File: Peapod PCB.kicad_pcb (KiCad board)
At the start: 2 copper layers, 16 parts, among them J1 CONN_01X01, J2 CONN_01X02, J3 CONN_01X06, J5 CONN_01X01, J6 CONN_01X01, J7 CONN_01X02, U1 ESP8266

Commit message: Changed main file for layout
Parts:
- moved BT1 38.2 mm to (193.0, 39.4)
- moved J1 35.6 mm to (179.1, 30.5)
- moved BTN1 22.2 mm to (182.9, 48.3), turned to 180 degrees
- moved BTN3 21.6 mm to (190.5, 48.3), turned to 180 degrees
- moved R3 21.0 mm to (205.7, 43.2), turned to 180 degrees
- moved R5 18.9 mm to (205.7, 38.1)
- moved J7 17.7 mm to (200.7, 48.9)
- moved R4 13.1 mm to (205.7, 40.6)
- moved R2 11.7 mm to (179.1, 39.4)
- moved J6 11.0 mm to (210.2, 48.9)
- moved J3 9.09 mm to (218.4, 31.1), turned to 270 degrees
- moved J5 8.47 mm to (216.5, 48.9)
- moved R1 7.41 mm to (179.1, 35.6)
- moved BTN2 3.81 mm to (175.3, 48.3), turned to 180 degrees
- moved J2 2.84 mm to (168.9, 30.5)
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
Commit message: changed things
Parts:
- moved BTN2 6.35 mm to (168.9, 48.3)
- moved BTN1 3.81 mm to (179.1, 48.3)
- moved BTN3 1.27 mm to (189.2, 48.3)
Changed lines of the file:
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@@
   )
   (module mod:Pushbutton (layer F.Cu)
-    (at 182.88 48.26 180)
+    (at 179.07 48.26 180)
     (fp_text reference BTN1 (at 0 0.5 180) (layer F.SilkS)
       (effects (font (size 1 1) (thickness 0.15)))
@@
   )
   (module mod:Pushbutton (layer F.Cu)
-    (at 175.26 48.26 180)
+    (at 168.91 48.26 180)
     (fp_text reference BTN2 (at 0 0.5 180) (layer F.SilkS)
       (effects (font (size 1 1) (thickness 0.15)))
@@
   )
   (module mod:Pushbutton (layer F.Cu)
-    (at 190.5 48.26 180)
+    (at 189.23 48.26 180)
     (fp_text reference BTN3 (at 0 0.5 180) (layer F.SilkS)
       (effects (font (size 1 1) (thickness 0.15)))

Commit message: made vias and tracks
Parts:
- moved J7 11.4 mm to (189.2, 49.5)
- moved J6 10.8 mm to (199.4, 49.5)
- moved BTN3 10.2 mm to (179.1, 47.0)
- moved J5 9.55 mm to (207.0, 49.5)
- moved BTN2 8.98 mm to (170.2, 39.4)
- moved BTN1 8.98 mm to (170.2, 47.0)
- moved R5 5.08 mm to (205.7, 43.2)
- moved BT1 5.08 mm to (188.0, 39.4)
- moved R3 2.54 mm to (205.7, 40.6)
- moved R4 2.54 mm to (205.7, 38.1)
- moved J3 2.29 mm to (217.2, 33.0)
- moved J2 1.27 mm to (170.2, 30.5)
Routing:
- net +3V3: track 0.00 -> 94.8 mm
- net Net-(J5-Pad1): track 0.00 -> 72.5 mm, vias 0 -> 2
- net Net-(BTN1-Pad2): track 0.00 -> 21.5 mm, vias 0 -> 2
- net Net-(J6-Pad1): track 0.00 -> 20.8 mm, vias 0 -> 2
- net Net-(J7-Pad1): track 0.00 -> 19.5 mm
- net Net-(BTN2-Pad2): track 0.00 -> 17.6 mm
- net Net-(R1-Pad1): track 0.00 -> 15.4 mm, vias 0 -> 2
- net Net-(J3-Pad4): track 0.00 -> 13.0 mm, vias 0 -> 2
- net Net-(J3-Pad5): track 0.00 -> 11.4 mm
- net Net-(BTN3-Pad2): track 0.00 -> 11.1 mm, vias 0 -> 2
- net Net-(J1-Pad1): track 0.00 -> 5.64 mm, vias 0 -> 1

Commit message: made fill zones
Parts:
- turned R1 to 180 degrees
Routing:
- net (no net): track 0.00 -> 31.4 mm
- net Net-(J5-Pad1): track 72.5 -> 58.9 mm
- net Net-(R1-Pad1): track 15.4 -> 1.81 mm, vias 2 -> 0
- net Net-(R5-Pad1): track 0.00 -> 5.83 mm
- net Net-(R3-Pad2): track 0.00 -> 5.56 mm
- net Net-(J7-Pad1): track 19.5 -> 24.8 mm
- net Net-(J2-Pad1): track 0.00 -> 1.27 mm
- net Net-(J1-Pad1): vias 1 -> 0
- added copper zone on F.Cu, net GND

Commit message: fixed stuff
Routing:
- net Net-(R1-Pad1): track 1.81 -> 13.8 mm, vias 0 -> 1
- net (no net): track 31.4 -> 21.2 mm
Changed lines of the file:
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@@
   (general
     (links 40)
-    (no_connects 18)
+    (no_connects 17)
     (area 154.9176 20.282599 222.719902 54.8674)
     (thickness 1.6002)
     (drawings 0)
-    (tracks 88)
+    (tracks 92)
     (zones 0)
     (modules 16)
@@
     )
   )
-  (segment (start 177.8 39.37) (end 177.8 38.1) (width 0.635) (layer B.Cu) (net 0))
-  (segment (start 177.8 38.1) (end 184.15 31.75) (width 0.635) (layer B.Cu) (net 0))
   (segment (start 185.42 29.21) (end 185.42 35.56) (width 0.635) (layer B.Cu) (net 0))
   (segment (start 180.34 30.48) (end 185.42 35.56) (width 0.635) (layer B.Cu) (net 0))
@@
   (segment (start 192.31 37.21) (end 199.42 37.21) (width 0.635) (layer F.Cu) (net 14))
   (segment (start 192.23 37.29) (end 192.31 37.21) (width 0.635) (layer F.Cu) (net 14))
-  (segment (start 183.61 31.21) (end 185.42 31.21) (width 0.635) (layer F.Cu) (net 15))
+  (segment (start 185.42 31.21) (end 182.975 31.21) (width 0.635) (layer F.Cu) (net 15) (status 400000))
+  (segment (start 182.245 35.56) (end 180.42 35.56) (width 0.635) (layer F.Cu) (net 15) (status 800000))
+  (segment (start 182.245 31.94) (end 182.245 35.56) (width 0.635) (layer F.Cu) (net 15))
+  (segment (start 182.975 31.21) (end 182.245 31.94) (width 0.635) (layer F.Cu) (net 15))
+  (via (at 180.42 35.56) (size 0.6858) (drill 0.3302) (layers F.Cu B.Cu) (net 15) (status C00000))
+  (segment (start 180.42 35.56) (end 177.8 38.18) (width 0.635) (layer B.Cu) (net 15) (status 400000))
+  (segment (start 177.8 38.18) (end 177.8 39.37) (width 0.635) (layer B.Cu) (net 15))
   (segment (start 204.39 40.64) (end 203.2 40.64) (width 0.635) (layer F.Cu) (net 16))
   (segment (start 201.77 39.21) (end 199.42 39.21) (width 0.635) (layer F.Cu) (net 16))

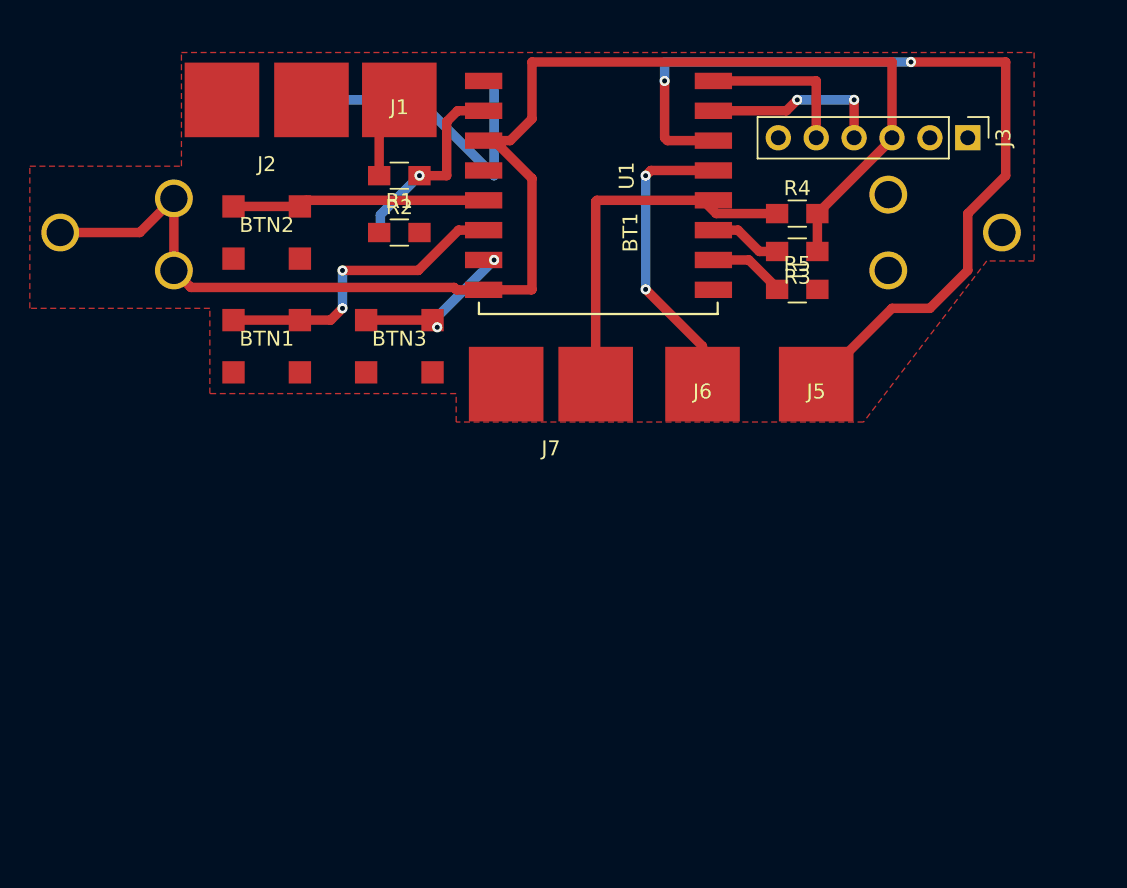
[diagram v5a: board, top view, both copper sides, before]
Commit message: Moved routing on the lines
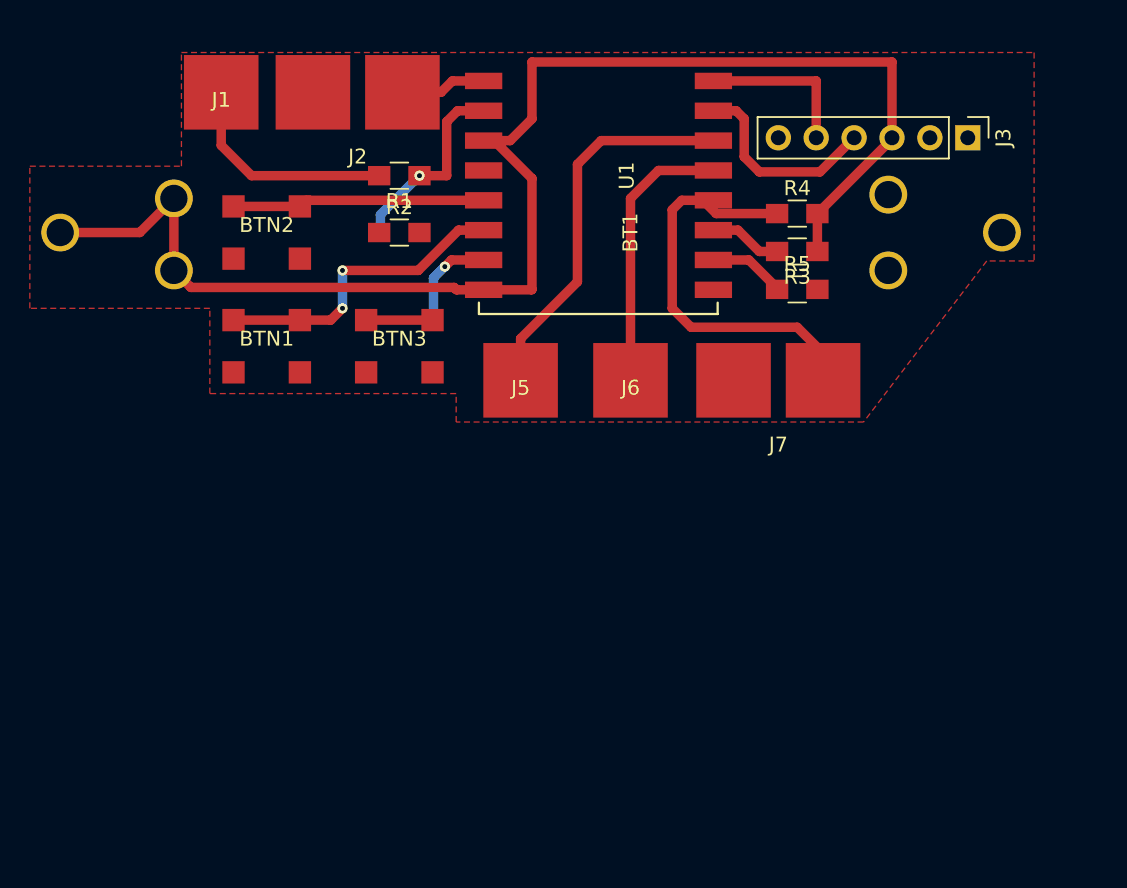
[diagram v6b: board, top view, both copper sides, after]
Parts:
- moved J5 19.8 mm to (187.2, 49.3)
- moved J7 15.2 mm to (204.5, 49.3)
- moved J1 11.9 mm to (167.1, 30.0)
- moved J2 6.12 mm to (176.3, 30.0)
- moved J6 4.83 mm to (194.6, 49.3)
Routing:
- net Net-(J5-Pad1): track 58.9 -> 25.1 mm, vias 2 -> 0
- net (no net): track 21.2 -> 0.00 mm
- net Net-(J1-Pad1): track 5.64 -> 16.9 mm
- net Net-(J2-Pad1): track 1.27 -> 7.73 mm
- net Net-(J7-Pad1): track 24.8 -> 27.4 mm
- net Net-(J6-Pad1): track 20.8 -> 19.1 mm, vias 2 -> 0
- net Net-(J3-Pad4): track 13.0 -> 14.3 mm, vias 2 -> 0
- net Net-(BTN3-Pad2): track 11.1 -> 11.6 mm, vias 2 -> 1

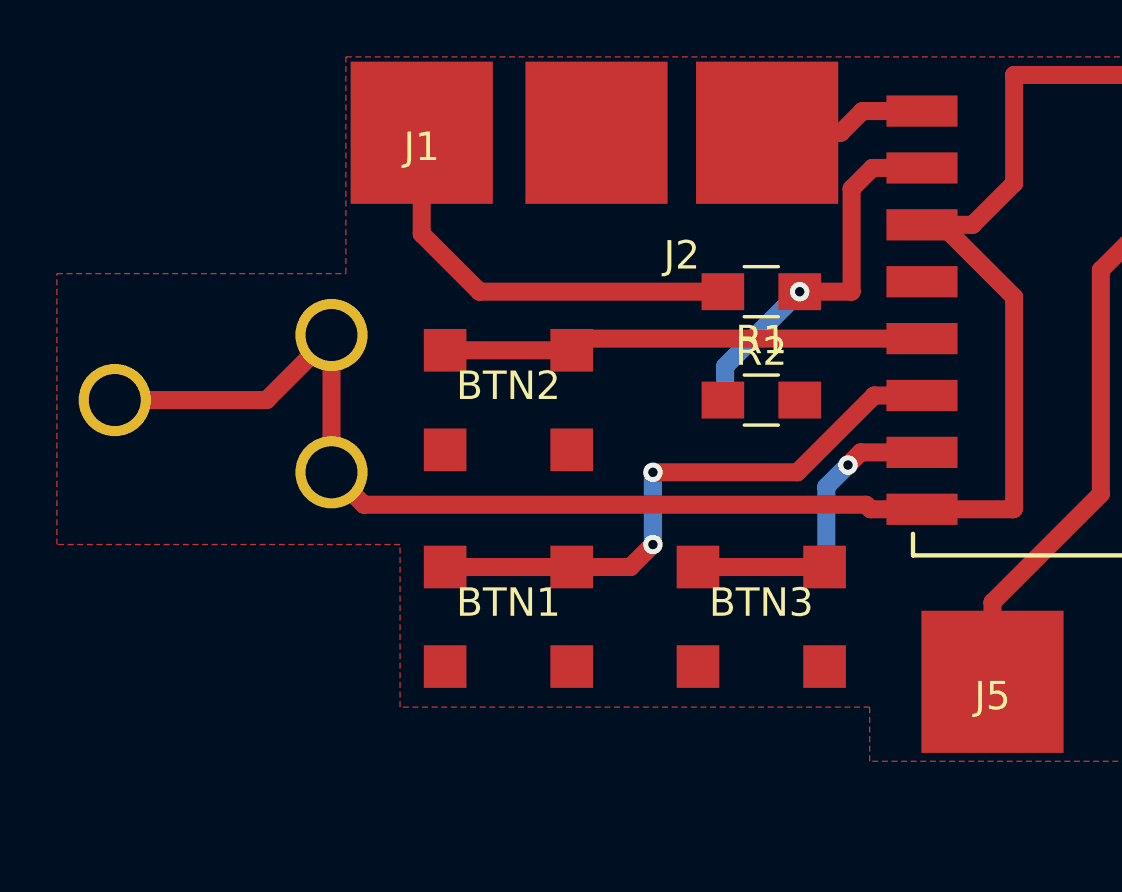
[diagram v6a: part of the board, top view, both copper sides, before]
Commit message: got rid of most vias
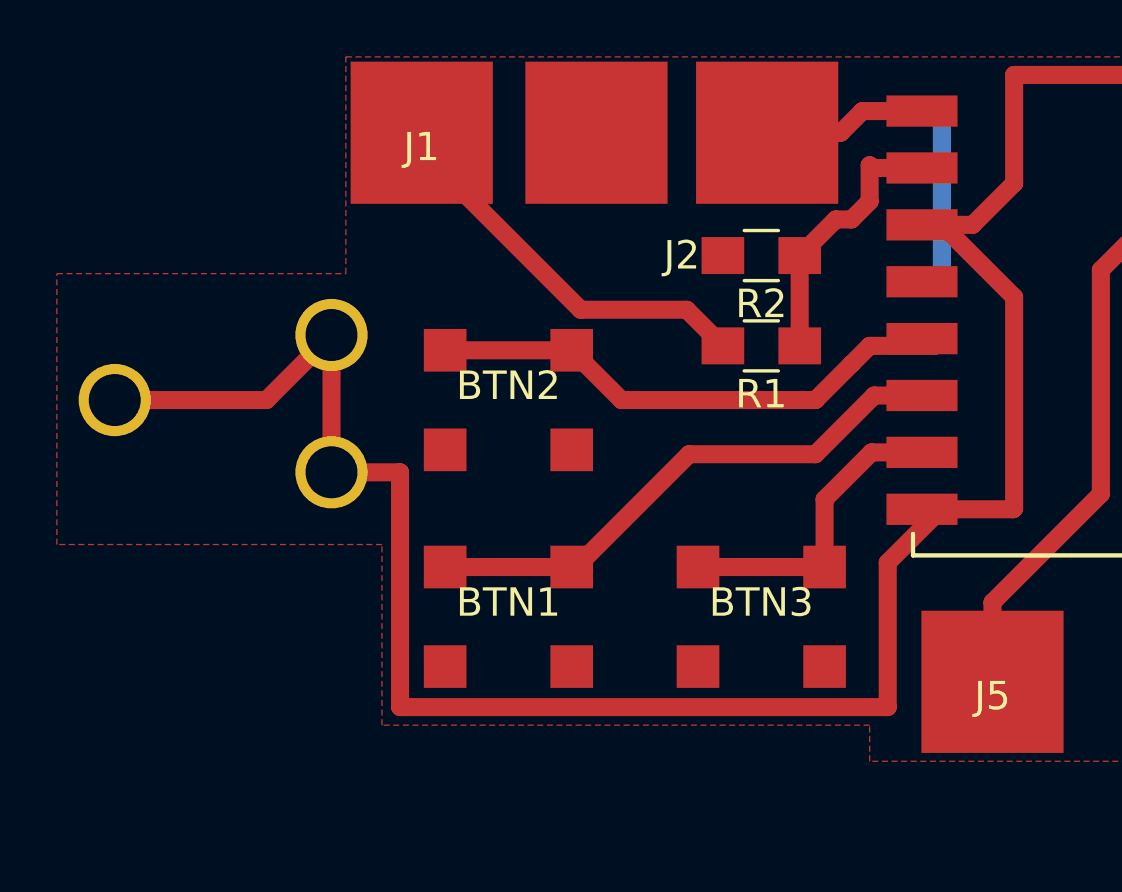
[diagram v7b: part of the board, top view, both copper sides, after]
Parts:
- moved R2 5.08 mm to (179.1, 34.3), turned to 180 degrees
- moved R1 1.91 mm to (179.1, 37.5)
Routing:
- net +3V3: track 94.8 -> 108.4 mm
- net (no net): track 0.00 -> 5.71 mm
- net Net-(R1-Pad1): track 13.8 -> 10.3 mm, vias 1 -> 0
- net Net-(J1-Pad1): track 16.9 -> 14.1 mm
- net Net-(BTN1-Pad2): track 21.5 -> 20.0 mm, vias 2 -> 0
- net Net-(BTN2-Pad2): track 17.6 -> 19.1 mm
- net Net-(BTN3-Pad2): track 11.6 -> 11.5 mm, vias 1 -> 0

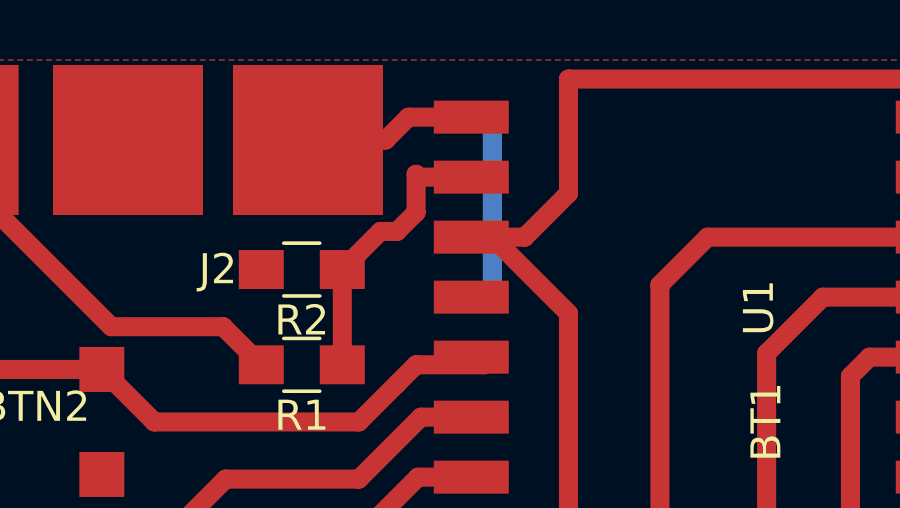
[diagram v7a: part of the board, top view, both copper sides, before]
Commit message: Changed Via
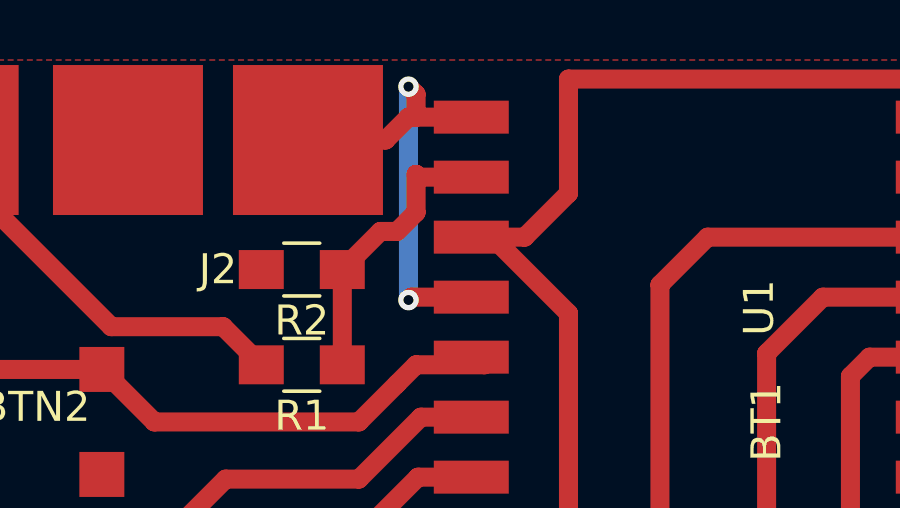
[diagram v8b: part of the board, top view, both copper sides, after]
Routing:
- net Net-(J2-Pad1): track 7.73 -> 18.8 mm, vias 0 -> 2
- net (no net): track 5.71 -> 0.00 mm
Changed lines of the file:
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@@
   (general
     (links 40)
-    (no_connects 15)
+    (no_connects 4)
     (area 154.305 20.282599 221.615001 54.6134)
     (thickness 1.6002)
     (drawings 0)
-    (tracks 86)
+    (tracks 93)
     (zones 0)
     (modules 16)
@@
     )
   )
-  (segment (start 185.42 29.21) (end 185.42 34.925) (width 0.635) (layer B.Cu) (net 0))
   (segment (start 163.96 41.91) (end 166.37 41.91) (width 0.635) (layer F.Cu) (net 1))
   (segment (start 183.515 45.085) (end 185.39 43.21) (width 0.635) (layer F.Cu) (net 1))
@@
   (segment (start 176.53 41.275) (end 180.975 41.275) (width 0.635) (layer F.Cu) (net 3))
   (segment (start 172.405 45.24) (end 167.955 45.24) (width 0.635) (layer F.Cu) (net 3))
-  (segment (start 167.955 37.62) (end 172.405 37.62) (width 0.635) (layer F.Cu) (net 4) (status C00000))
-  (segment (start 172.405 37.62) (end 174.155 39.37) (width 0.635) (layer F.Cu) (net 4) (status 400000))
+  (segment (start 167.955 37.62) (end 172.405 37.62) (width 0.635) (layer F.Cu) (net 4))
+  (segment (start 172.405 37.62) (end 174.155 39.37) (width 0.635) (layer F.Cu) (net 4))
   (segment (start 174.155 39.37) (end 180.975 39.37) (width 0.635) (layer F.Cu) (net 4))
   (segment (start 180.975 39.37) (end 182.245 38.1) (width 0.635) (layer F.Cu) (net 4))
   (segment (start 182.245 38.1) (end 182.88 37.465) (width 0.635) (layer F.Cu) (net 4))
-  (segment (start 182.88 37.465) (end 185.165 37.465) (width 0.635) (layer F.Cu) (net 4) (status 800000))
-  (segment (start 185.165 37.465) (end 185.42 37.21) (width 0.635) (layer F.Cu) (net 4) (status C00000))
+  (segment (start 182.88 37.465) (end 185.165 37.465) (width 0.635) (layer F.Cu) (net 4))
+  (segment (start 185.165 37.465) (end 185.42 37.21) (width 0.635) (layer F.Cu) (net 4))
   (segment (start 181.295 45.24) (end 181.295 42.86) (width 0.635) (layer F.Cu) (net 5))
   (segment (start 182.945 41.21) (end 185.42 41.21) (width 0.635) (layer F.Cu) (net 5))
   (segment (start 181.295 42.86) (end 182.945 41.21) (width 0.635) (layer F.Cu) (net 5))
   (segment (start 181.13 45.24) (end 176.845 45.24) (width 0.635) (layer F.Cu) (net 5))
-  (segment (start 167.132 29.972) (end 167.132 30.607) (width 0.635) (layer F.Cu) (net 6) (status C00000))
-  (segment (start 167.132 30.607) (end 172.72 36.195) (width 0.635) (layer F.Cu) (net 6) (status 400000))
+  (segment (start 167.132 29.972) (end 167.132 30.607) (width 0.635) (layer F.Cu) (net 6))
+  (segment (start 167.132 30.607) (end 172.72 36.195) (width 0.635) (layer F.Cu) (net 6))
   (segment (start 172.72 36.195) (end 176.45 36.195) (width 0.635) (layer F.Cu) (net 6))
-  (segment (start 176.45 36.195) (end 177.72 37.465) (width 0.635) (layer F.Cu) (net 6) (status 800000))
+  (segment (start 176.45 36.195) (end 177.72 37.465) (width 0.635) (layer F.Cu) (net 6))
+  (segment (start 182.88 29.21) (end 182.88 28.448) (width 0.635) (layer F.Cu) (net 7))
+  (segment (start 182.722 35.21) (end 185.42 35.21) (width 0.635) (layer F.Cu) (net 7))
+  (segment (start 182.626 35.306) (end 182.722 35.21) (width 0.635) (layer F.Cu) (net 7))
+  (via (at 182.626 35.306) (size 0.6858) (drill 0.3302) (layers F.Cu B.Cu) (net 7))
+  (segment (start 182.626 28.194) (end 182.626 35.306) (width 0.635) (layer B.Cu) (net 7))
+  (via (at 182.626 28.194) (size 0.6858) (drill 0.3302) (layers F.Cu B.Cu) (net 7))
+  (segment (start 182.88 28.448) (end 182.626 28.194) (width 0.635) (layer F.Cu) (net 7))
   (segment (start 179.276 29.972) (end 181.864 29.972) (width 0.635) (layer F.Cu) (net 7))
-  (segment (start 182.626 29.21) (end 185.42 29.21) (width 0.635) (layer F.Cu) (net 7))
+  (segment (start 182.626 29.21) (end 182.88 29.21) (width 0.635) (layer F.Cu) (net 7))
+  (segment (start 182.88 29.21) (end 185.42 29.21) (width 0.635) (layer F.Cu) (net 7))
   (segment (start 181.864 29.972) (end 182.626 29.21) (width 0.635) (layer F.Cu) (net 7))
   (segment (start 185.42 29.21) (end 184.15 29.21) (width 0.635) (layer F.Cu) (net 7))
@@
   (segment (start 204.39 38.1) (end 200.31 38.1) (width 0.635) (layer F.Cu) (net 14))
   (segment (start 200.31 38.1) (end 199.42 37.21) (width 0.635) (layer F.Cu) (net 14))
-  (segment (start 180.42 37.465) (end 180.42 34.29) (width 0.635) (layer F.Cu) (net 15) (status C00000))
-  (segment (start 180.42 34.29) (end 181.69 33.02) (width 0.635) (layer F.Cu) (net 15) (status 400000))
+  (segment (start 180.42 37.465) (end 180.42 34.29) (width 0.635) (layer F.Cu) (net 15))
+  (segment (start 180.42 34.29) (end 181.69 33.02) (width 0.635) (layer F.Cu) (net 15))
   (segment (start 181.69 33.02) (end 182.245 33.02) (width 0.635) (layer F.Cu) (net 15))
   (segment (start 182.245 33.02) (end 182.88 32.385) (width 0.635) (layer F.Cu) (net 15))
   (segment (start 182.88 32.385) (end 182.88 31.115) (width 0.635) (layer F.Cu) (net 15))
   (segment (start 182.88 31.115) (end 182.975 31.21) (width 0.635) (layer F.Cu) (net 15))
-  (segment (start 182.975 31.21) (end 185.42 31.21) (width 0.635) (layer F.Cu) (net 15) (status 800000))
+  (segment (start 182.975 31.21) (end 185.42 31.21) (width 0.635) (layer F.Cu) (net 15))
   (segment (start 204.39 40.64) (end 203.2 40.64) (width 0.635) (layer F.Cu) (net 16))
   (segment (start 201.77 39.21) (end 199.42 39.21) (width 0.635) (layer F.Cu) (net 16))
@@
     (connect_pads (clearance 0.508))
     (min_thickness 0.254)
-    (fill (arc_segments 16) (thermal_gap 0.508) (thermal_bridge_width 0.508))
+    (fill yes (arc_segments 16) (thermal_gap 0.508) (thermal_bridge_width 0.508))
     (polygon
       (pts
